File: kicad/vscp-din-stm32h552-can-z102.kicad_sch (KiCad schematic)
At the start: 0 parts

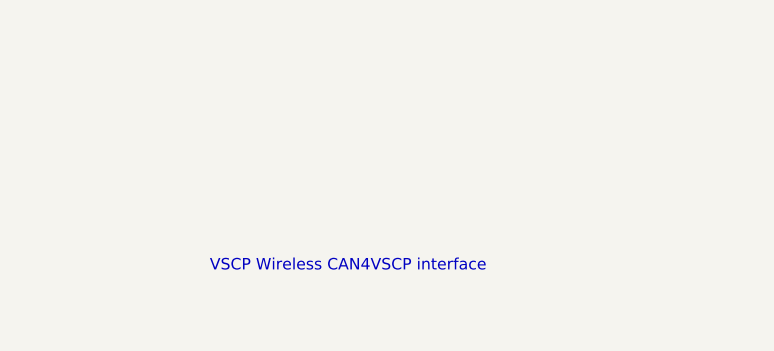
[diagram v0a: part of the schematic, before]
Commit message: Fixed power issue
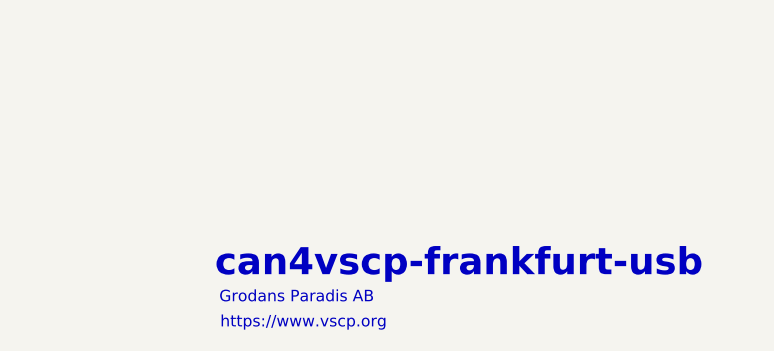
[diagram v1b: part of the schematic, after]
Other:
- note added: "Grodans Paradis AB"
- note added: "can4vscp-frankfurt-usb"
- note added: "https://www.vscp.org"
- note removed: "VSCP Wireless CAN4VSCP interface"
- title: vscp-din-esp32-can-z102 -> can4vscp-frankfurt-usb
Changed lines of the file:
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@@
 	(paper "A4")
 	(title_block
-		(title "vscp-din-esp32-can-z102")
-		(rev "C")
+		(title "can4vscp-frankfurt-usb")
+		(date "2020-06-04")
+		(rev "A")
 		(company "Grodans Paradis AB")
+		(comment 1 "https://www.vscp.org")
 	)
-	(text "VSCP Wireless CAN4VSCP interface"
+	(text "https://www.vscp.org"
 		(exclude_from_sim no)
-		(at 179.07 170.18 0)
+		(at 189.484 175.768 0)
 		(effects
 			(font
 				(size 1.27 1.27)
 			)
-			(justify left bottom)
 		)
 	)
+	(text "can4vscp-frankfurt-usb"
+		(exclude_from_sim no)
+		(at 206.756 169.164 0)
+		(effects
+			(font
+				(size 3 3)
+				(thickness 0.6)
+				(bold yes)
+			)
+		)
+	)
+	(text "Grodans Paradis AB"
+		(exclude_from_sim no)
+		(at 188.722 172.974 0)
+		(effects
+			(font
+				(size 1.27 1.27)
+			)
+		)
+	)
